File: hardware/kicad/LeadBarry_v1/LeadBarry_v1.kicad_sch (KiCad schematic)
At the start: 0 parts

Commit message: fix: start up the schematic
off course nothing done yet))
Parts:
- added U1: PicoW, RPi_PicoW:RPi_Pico_SMD_TH, symbol RPi_PicoW:PicoW
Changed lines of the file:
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@@
 	(generator_version "8.0")
 	(paper "A4")
+	(symbol
+		(lib_id "RPi_PicoW:PicoW")
+		(at 82.55 87.63 0)
+		(unit 1)
+		(exclude_from_sim no)
+		(in_bom yes)
+		(on_board yes)
+		(dnp no)
+		(fields_autoplaced yes)
+		(property "Reference" "U1"
+			(at 82.55 55.88 0)
+			(effects
+				(font
+					(size 1.27 1.27)
+				)
+			)
+		)
+		(property "Value" "PicoW"
+			(at 82.55 58.42 0)
+			(effects
+				(font
+					(size 1.27 1.27)
+				)
+			)
+		)
+		(property "Footprint" "RPi_PicoW:RPi_Pico_SMD_TH"
+			(at 82.55 87.63 90)
+			(effects
+				(font
+					(size 1.27 1.27)
+				)
+				(hide yes)
+			)
+		)
+		(property "Datasheet" ""
+			(at 82.55 87.63 0)
+			(effects
+				(font
+					(size 1.27 1.27)
+				)
+				(hide yes)
+			)
+		)
+		(property "Description" ""
+			(at 82.55 87.63 0)
+			(effects
+				(font
+					(size 1.27 1.27)
+				)
+				(hide yes)
+			)
+		)
+		(pin "38"
+		)
+		(pin "39"
+		)
+		(pin "12"
+		)
+		(pin "11"
+		)
+		(pin "8"
+		)
+		(pin "9"
+		)
+		(pin "16"
+		)
+		(pin "17"
+		)
+		(pin "18"
+		)
+		(pin "19"
+		)
+		(pin "1"
+		)
+		(pin "10"
+		)
+		(pin "43"
+		)
+		(pin "5"
+		)
+		(pin "30"
+		)
+		(pin "31"
+		)
+		(pin "14"
+		)
+		(pin "15"
+		)
+		(pin "6"
+		)
+		(pin "7"
+		)
+		(pin "36"
+		)
+		(pin "37"
+		)
+		(pin "21"
+		)
+		(pin "22"
+		)
+		(pin "27"
+		)
+		(pin "28"
+		)
+		(pin "34"
+		)
+		(pin "35"
+		)
+		(pin "32"
+		)
+		(pin "33"
+		)
+		(pin "2"
+		)
+		(pin "20"
+		)
+		(pin "29"
+		)
+		(pin "3"
+		)
+		(pin "25"
+		)
+		(pin "26"
+		)
+		(pin "23"
+		)
+		(pin "24"
+		)
+		(pin "41"
+		)
+		(pin "42"
+		)
+		(pin "13"
+		)
+		(pin "4"
+		)
+		(pin "40"
+		)
+		(instances
+			(project ""
+				(path "/20771d85-0a47-48d4-b39f-5d01020408af"
+					(reference "U1")
+					(unit 1)
+				)
+			)
+		)
+	)
 	(sheet_instances
 		(path "/"

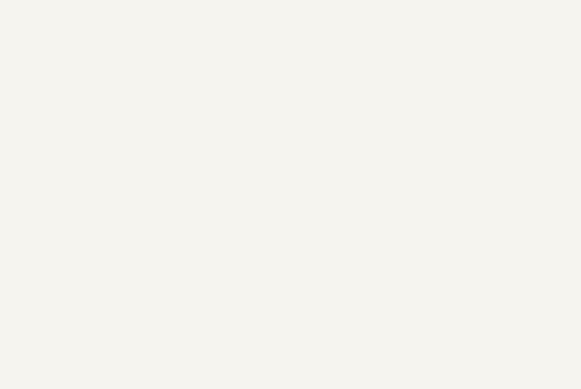
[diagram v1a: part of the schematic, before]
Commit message: fix: battery switch circuit + calculation
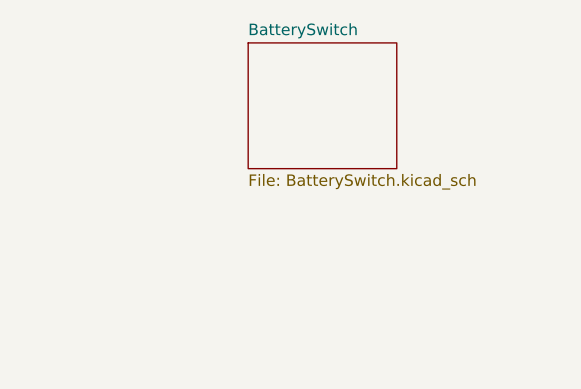
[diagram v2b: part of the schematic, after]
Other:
- added sheet BatterySwitch (BatterySwitch.kicad_sch)
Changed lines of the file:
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@@
+		)
+	)
+	(sheet
+		(at 166.37 29.21)
+		(size 16.51 13.97)
+		(fields_autoplaced yes)
+		(stroke
+			(width 0.1524)
+			(type solid)
+		)
+		(fill
+			(color 0 0 0 0.0000)
+		)
+		(property "Sheetname" "BatterySwitch"
+			(at 166.37 28.4984 0)
+			(effects
+				(font
+					(size 1.27 1.27)
+				)
+				(justify left bottom)
+			)
+		)
+		(property "Sheetfile" "BatterySwitch.kicad_sch"
+			(at 166.37 43.7646 0)
+			(effects
+				(font
+					(size 1.27 1.27)
+				)
+				(justify left top)
+			)
+		)
+		(instances
+			(project "LeadBarry_v1"
+				(path "/20771d85-0a47-48d4-b39f-5d01020408af"
+					(page "2")
+				)
+			)
 		)
 	)

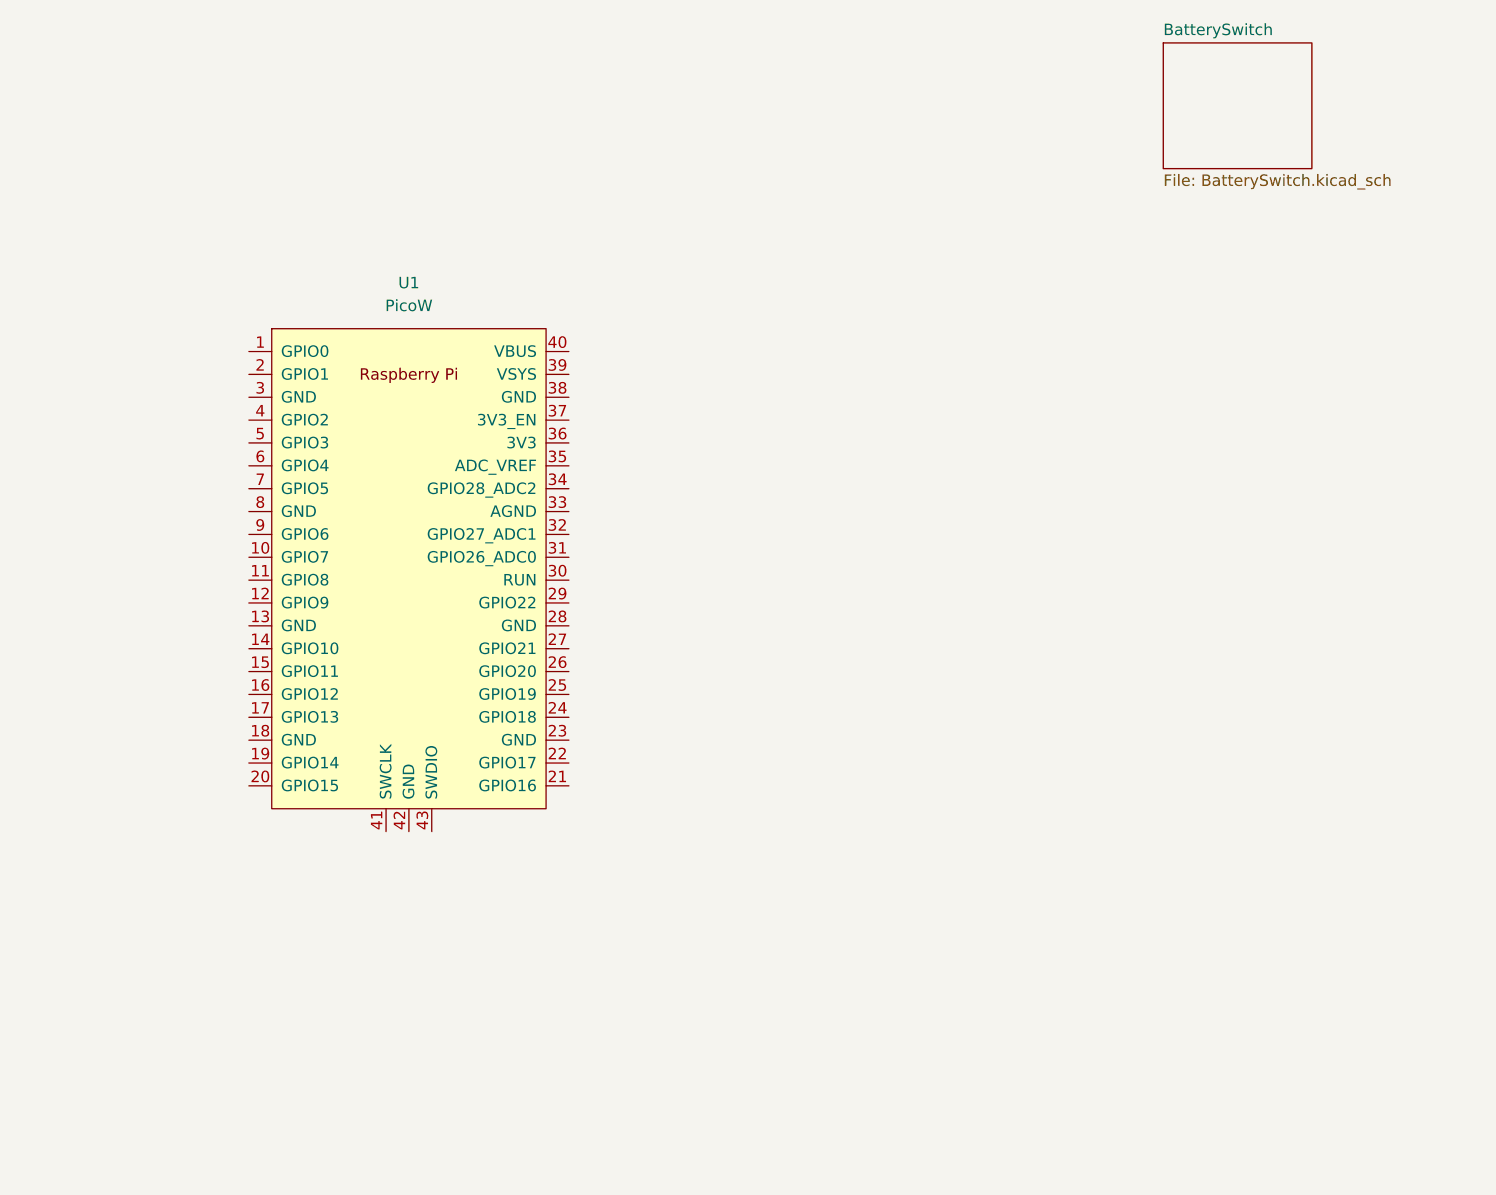
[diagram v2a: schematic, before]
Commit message: fix: P- -> B-, P+ -> P-
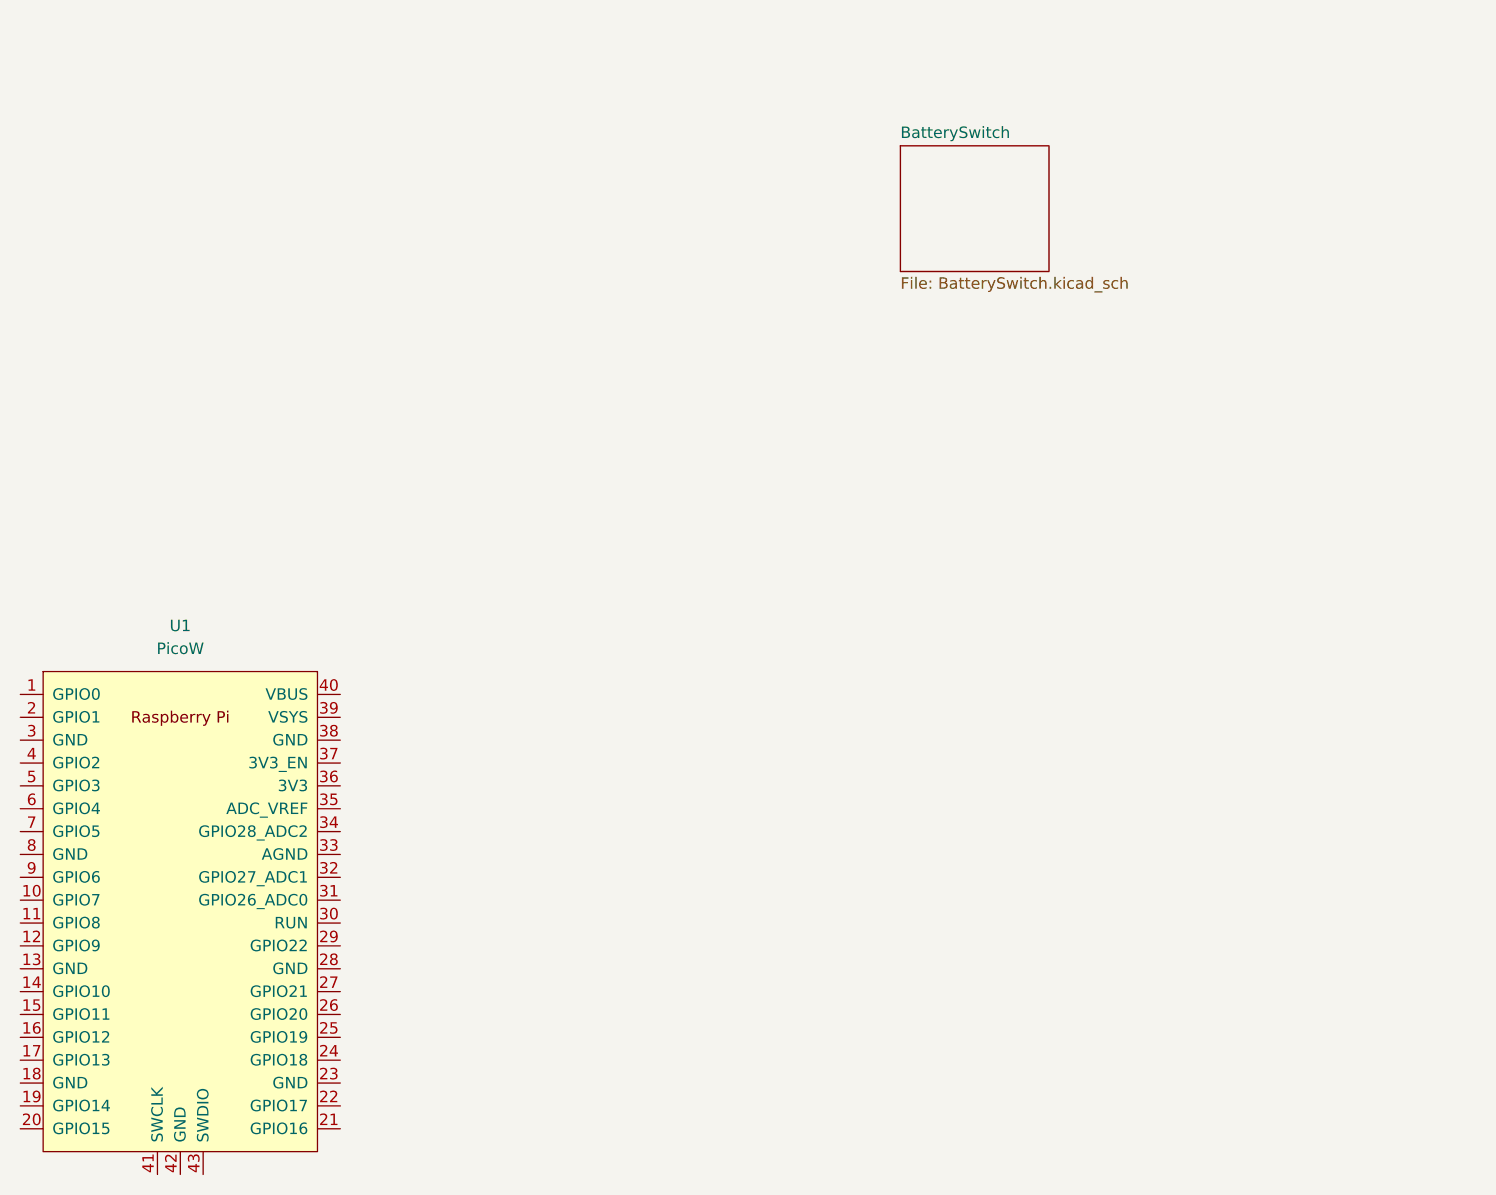
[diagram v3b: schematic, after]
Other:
- moved on the sheet: U1
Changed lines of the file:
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@@
 	(symbol
 		(lib_id "RPi_PicoW:PicoW")
-		(at 82.55 87.63 0)
+		(at 57.15 125.73 0)
 		(unit 1)
 		(exclude_from_sim no)
@@
 		(fields_autoplaced yes)
 		(property "Reference" "U1"
-			(at 82.55 55.88 0)
+			(at 57.15 93.98 0)
 			(effects
 				(font
@@
 		)
 		(property "Value" "PicoW"
-			(at 82.55 58.42 0)
+			(at 57.15 96.52 0)
 			(effects
 				(font
@@
 		)
 		(property "Footprint" "RPi_PicoW:RPi_Pico_SMD_TH"
-			(at 82.55 87.63 90)
+			(at 57.15 125.73 90)
 			(effects
 				(font
@@
 		)
 		(property "Datasheet" ""
-			(at 82.55 87.63 0)
+			(at 57.15 125.73 0)
 			(effects
 				(font
@@
 		)
 		(property "Description" ""
-			(at 82.55 87.63 0)
+			(at 57.15 125.73 0)
 			(effects
 				(font
@@
 	)
 	(sheet
-		(at 166.37 29.21)
+		(at 137.16 40.64)
 		(size 16.51 13.97)
 		(fields_autoplaced yes)
@@
 		)
 		(property "Sheetname" "BatterySwitch"
-			(at 166.37 28.4984 0)
+			(at 137.16 39.9284 0)
 			(effects
 				(font
@@
 		)
 		(property "Sheetfile" "BatterySwitch.kicad_sch"
-			(at 166.37 43.7646 0)
+			(at 137.16 55.1946 0)
 			(effects
 				(font

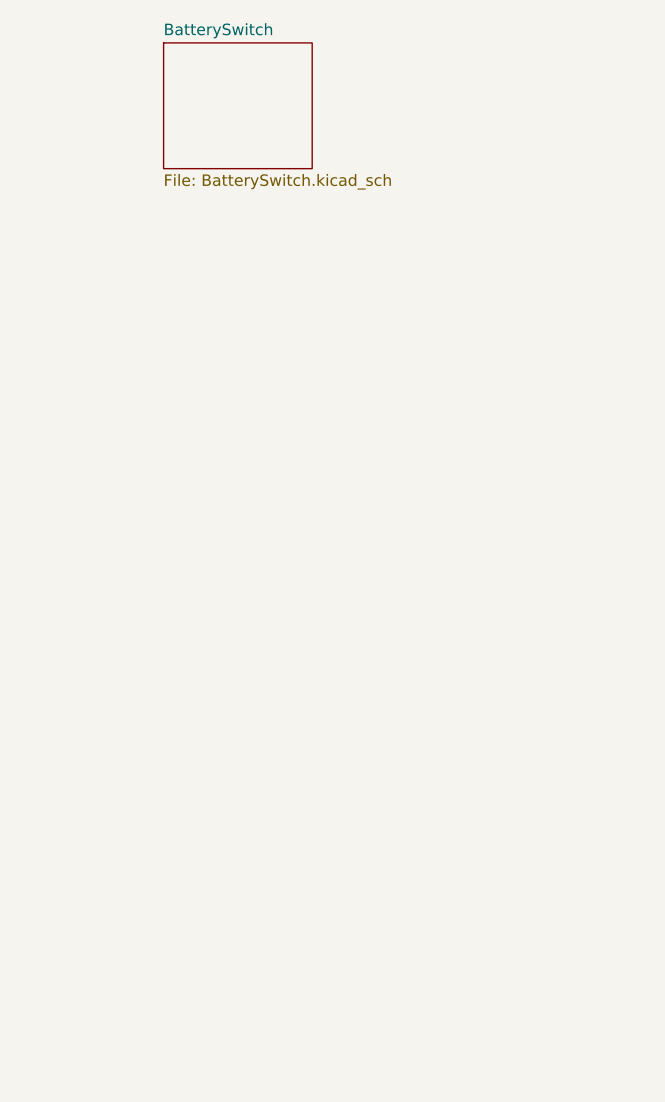
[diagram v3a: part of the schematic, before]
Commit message: fix: controlled dc-dc schema
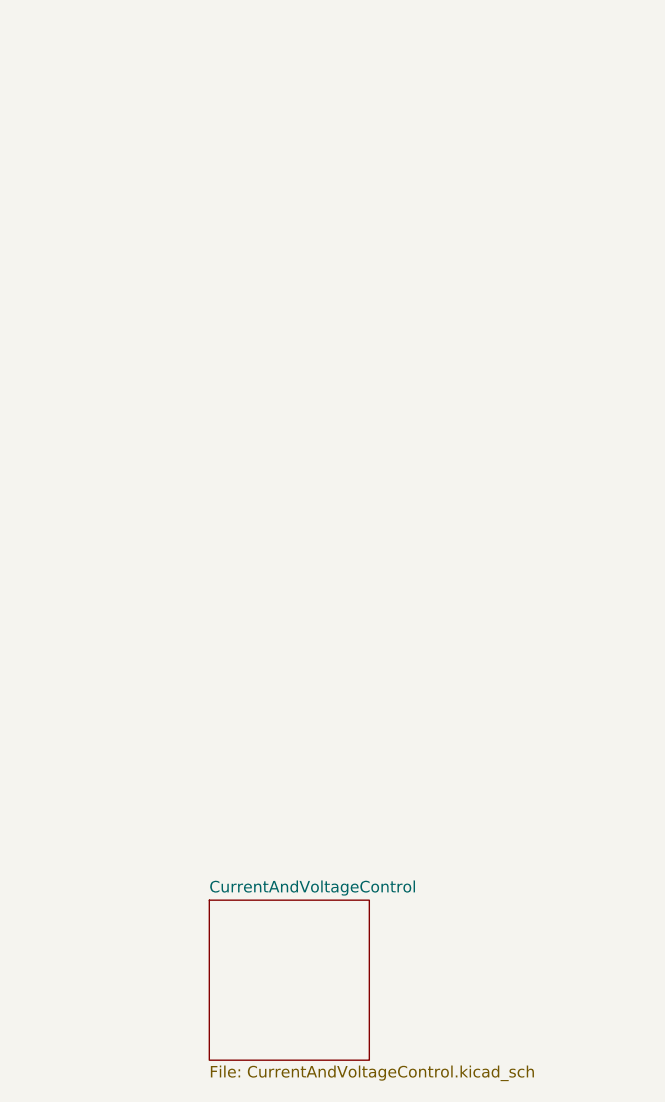
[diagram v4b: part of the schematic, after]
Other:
- removed sheet BatterySwitch
- added sheet CurrentAndVoltageControl (CurrentAndVoltageControl.kicad_sch)
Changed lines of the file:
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@@
 	)
 	(sheet
-		(at 137.16 40.64)
-		(size 16.51 13.97)
+		(at 142.24 135.89)
+		(size 17.78 17.78)
 		(fields_autoplaced yes)
 		(stroke
@@
 			(color 0 0 0 0.0000)
 		)
-		(property "Sheetname" "BatterySwitch"
-			(at 137.16 39.9284 0)
+		(property "Sheetname" "CurrentAndVoltageControl"
+			(at 142.24 135.1784 0)
 			(effects
 				(font
@@
 			)
 		)
-		(property "Sheetfile" "BatterySwitch.kicad_sch"
-			(at 137.16 55.1946 0)
+		(property "Sheetfile" "CurrentAndVoltageControl.kicad_sch"
+			(at 142.24 154.2546 0)
 			(effects
 				(font
@@
 			(project "LeadBarry_v1"
 				(path "/20771d85-0a47-48d4-b39f-5d01020408af"
-					(page "2")
+					(page "3")
 				)
 			)

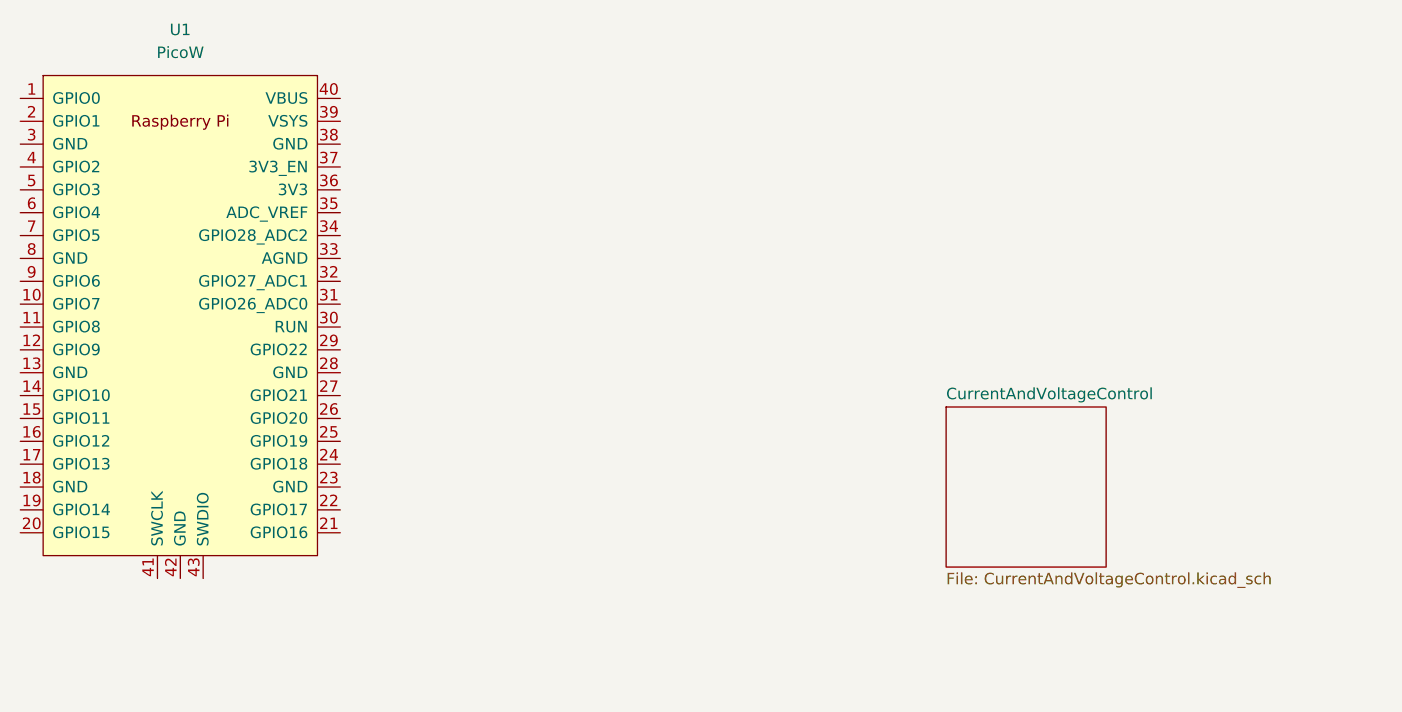
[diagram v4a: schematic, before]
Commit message: fix: schematic improvement
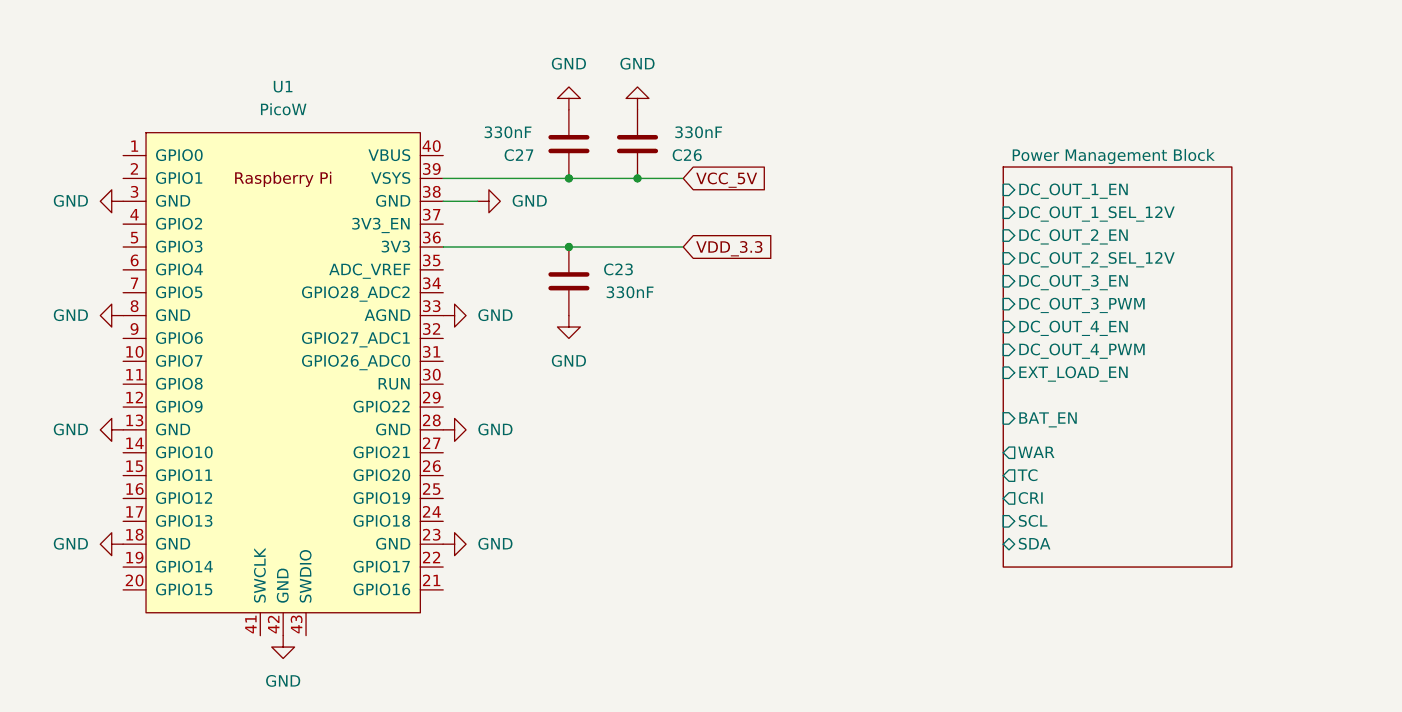
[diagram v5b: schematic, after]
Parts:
- added C23, C26, C27: 330nF, Capacitor_SMD:C_1206_3216Metric_Pad1.33x1.80mm_HandSolder, symbol Device:C
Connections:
- net GND: now reaches U1.13 (GND)
- net GND: now also U1.18 (GND), U1.23 (GND), U1.28 (GND), U1.3 (GND), U1.33 (AGND), U1.38 (GND), U1.42 (GND), U1.8 (GND), C23.2, C26.2, C27.2
- net VDD_3.3: now reaches U1.36 (3V3)
- net VDD_3.3: now also C23.1
- net VCC_5V: now reaches U1.39 (VSYS)
- net VCC_5V: now also C26.1, C27.1
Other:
- sheet CurrentAndVoltageControl renamed PowerManagementBlock
- sheet PowerManagementBlock ports: added BAT_EN, CRI, DC_OUT_1_EN, DC_OUT_1_SEL_12V, DC_OUT_2_EN, DC_OUT_2_SEL_12V, DC_OUT_3_EN, DC_OUT_3_PWM, DC_OUT_4_EN, DC_OUT_4_PWM, EXT_LOAD_EN, SCL, SDA, TC, WAR; removed none
- moved on the sheet: U1
